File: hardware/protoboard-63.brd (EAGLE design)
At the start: 195.6 x 63.5 mm, 161 parts

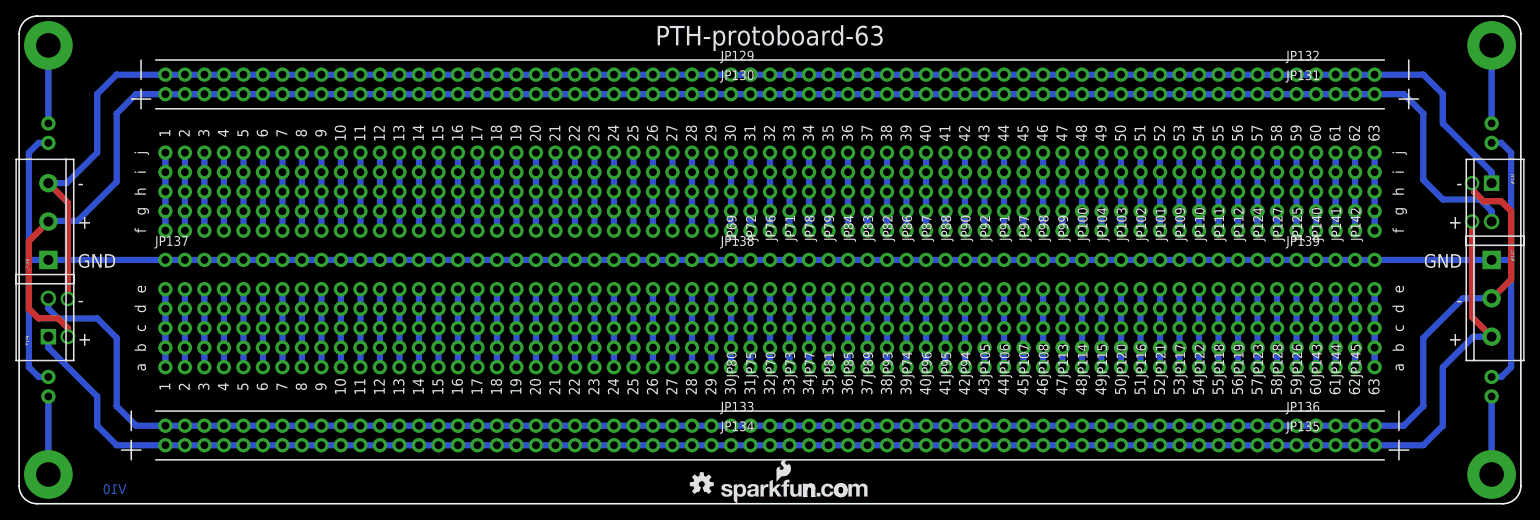
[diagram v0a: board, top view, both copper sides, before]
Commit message: Revision after group review.
-Changes to naming/branding.
-Added extra jumper option for 2-rails only operation.
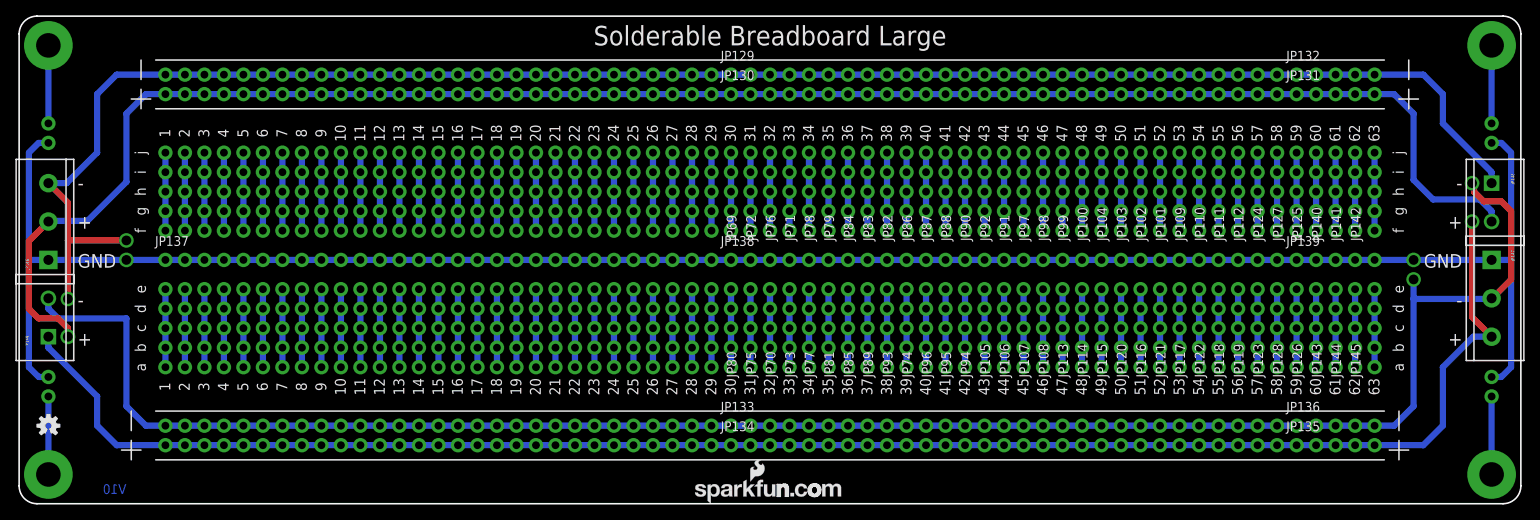
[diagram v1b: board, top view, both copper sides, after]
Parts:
- moved LOGO3 85.4 mm to (3.81, 10.2)
- moved LOGO2 3.43 mm to (88.0, 0.00)
- moved LOGO1 1.65 mm to (107.1, 0.00)
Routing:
- net V-TOP: track 223.3 -> 231.0 mm, vias 1 -> 2
- net V-BOT: track 232.5 -> 239.5 mm, vias 1 -> 2
- net GND: vias 0 -> 2
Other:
- board text added: "Solderable Breadboard Large"
- board text removed: "PTH-protoboard-63"
